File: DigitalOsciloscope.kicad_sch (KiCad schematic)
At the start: 0 parts

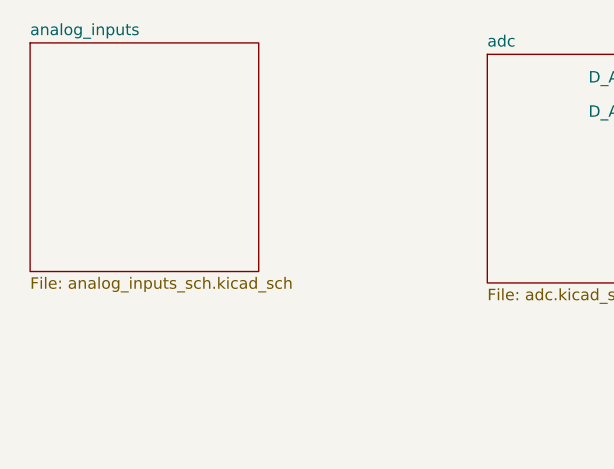
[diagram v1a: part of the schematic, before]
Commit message: Place most of the components in cart
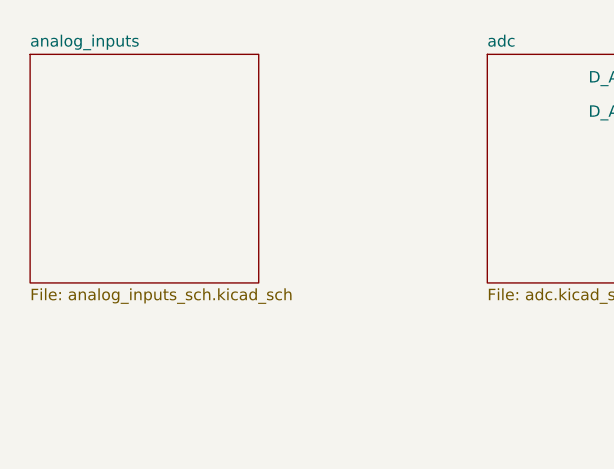
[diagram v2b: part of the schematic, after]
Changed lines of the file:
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@@
 	)
 	(sheet
-		(at 91.44 57.15)
+		(at 91.44 58.42)
 		(size 25.4 25.4)
 		(exclude_from_sim no)
@@
 		)
 		(property "Sheetname" "analog_inputs"
-			(at 91.44 56.4384 0)
+			(at 91.44 57.7084 0)
 			(effects
 				(font
@@
 		)
 		(property "Sheetfile" "analog_inputs_sch.kicad_sch"
-			(at 91.44 83.1346 0)
+			(at 91.44 84.4046 0)
 			(effects
 				(font
